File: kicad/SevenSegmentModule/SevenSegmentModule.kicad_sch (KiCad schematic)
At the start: 17 parts, among them J1 IN, J2 PIN, J4 OUT, J5 POUT, U1 TPIC6595

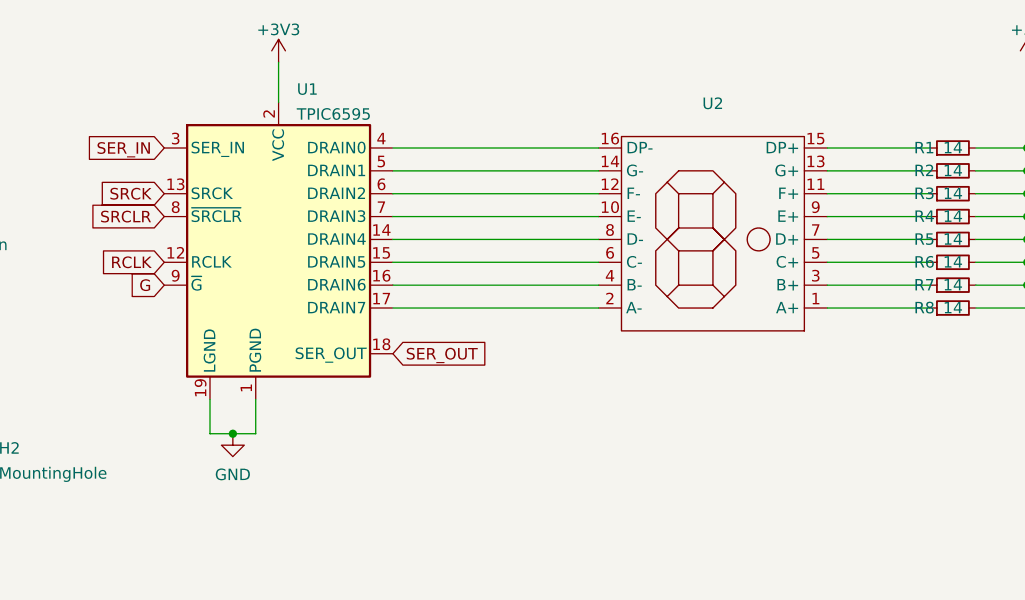
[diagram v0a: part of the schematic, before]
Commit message: Add modular PCBs and cleanup backups
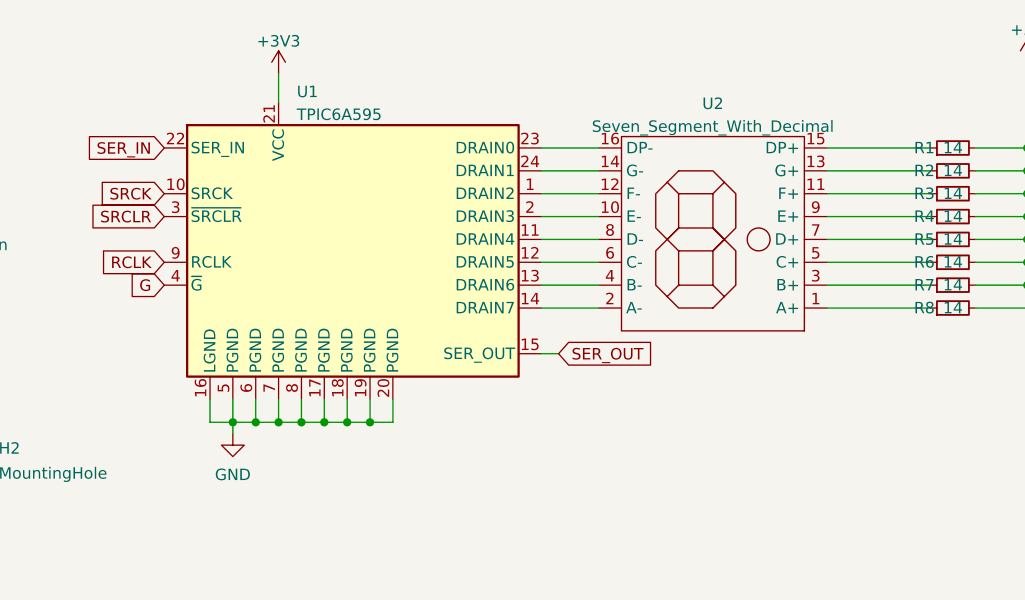
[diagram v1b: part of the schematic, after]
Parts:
- removed U1: TPIC6595, Package_SO:SOIC-20W_7.5x12.8mm_P1.27mm, symbol Interface_Expansion:TPIC6595
- added U1: TPIC6A595, Package_SO:SOIC-24W_7.5x15.4mm_P1.27mm, symbol Interface_Expansion:TPIC6A595
- U2: value (none) -> Seven_Segment_With_Decimal; footprint (none) -> LED_Filaments:Segen_Segment_69mm_with_dp
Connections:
- net +3V3: now also U1.21 (VCC)
- net G: now also U1.4 (~{G})
- net GND: now also U1.16 (LGND), U1.17 (PGND), U1.18 (PGND), U1.19 (PGND), U1.20 (PGND), U1.5 (PGND), U1.6 (PGND), U1.7 (PGND), U1.8 (PGND)
- net RCLK: now also U1.9 (RCLK)
- net SER_IN: now also U1.22 (SER_IN)
- net SER_OUT: now also U1.15 (SER_OUT)
- net SRCK: now also U1.10 (SRCK)
- net SRCLR: now also U1.3 (~{SRCLR})
- net at U2.8 (D-): now also U1.11 (DRAIN4)
- net at U2.6 (C-): now also U1.12 (DRAIN5)
- net at U2.4 (B-): now also U1.13 (DRAIN6)
- net at U2.2 (A-): now also U1.14 (DRAIN7)
- net at U2.16 (DP-): now also U1.23 (DRAIN0)
- net at U2.14 (G-): now also U1.24 (DRAIN1)
- net at U2.12 (F-): now also U1.1 (DRAIN2)
- net at U2.10 (E-): now also U1.2 (DRAIN3)
